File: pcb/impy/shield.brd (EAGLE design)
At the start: 133 x 107 mm, 117 parts, among them J1 USB-2410-06, J2 SI-60062-F, J3 5V, U1 AD5933YRS, U10 LTC3406AB, U11 23LCV1024-I/SN, U12 MIC2009A-1YM6, U13 ADG725BSU, U14 ADG725BSU, U2 ADG704BRM, U3 AD8656ARZ, U4 M24C08WMN, U5 ADG706BRU, U6 DP83848I, U7 MIC2009A-1YM6, U8 AT25DF081A-SS, U9 SST25VF080B-80-4I-S2

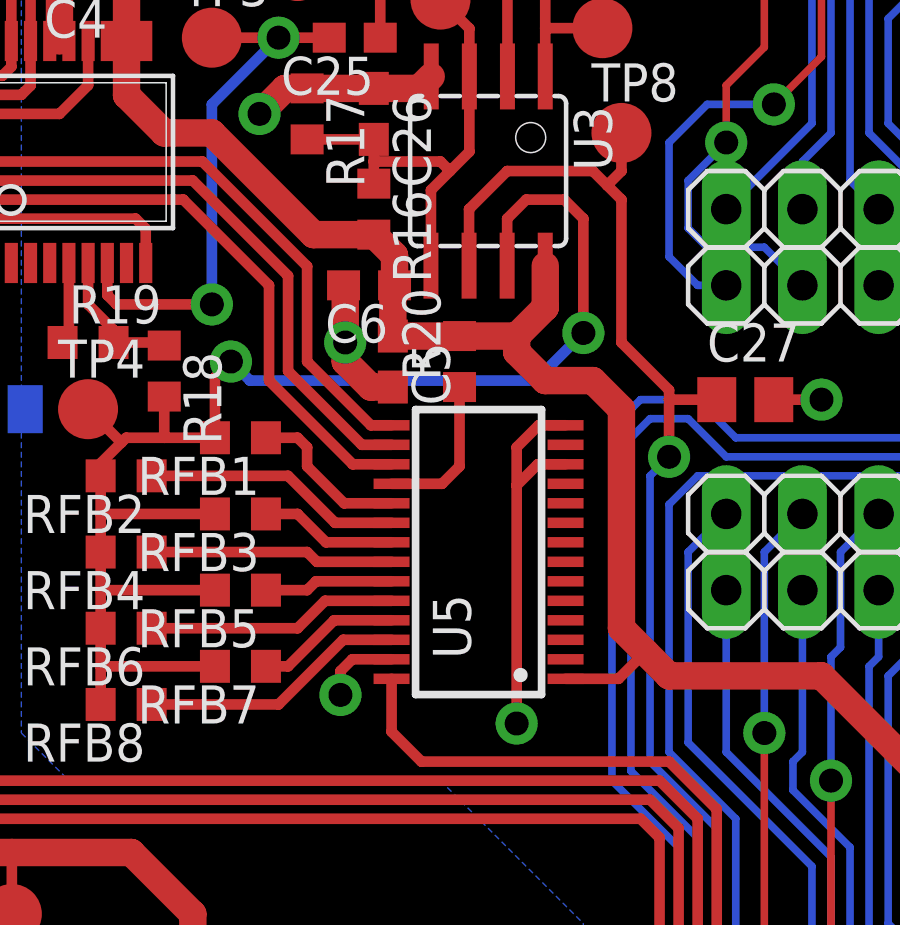
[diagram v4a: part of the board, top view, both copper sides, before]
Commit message: * pcb/impy: (shield.sch) Remove PE11 from discovery board header.   (shield.brd) Move some traces in preparation for feedback mux selection signal change.
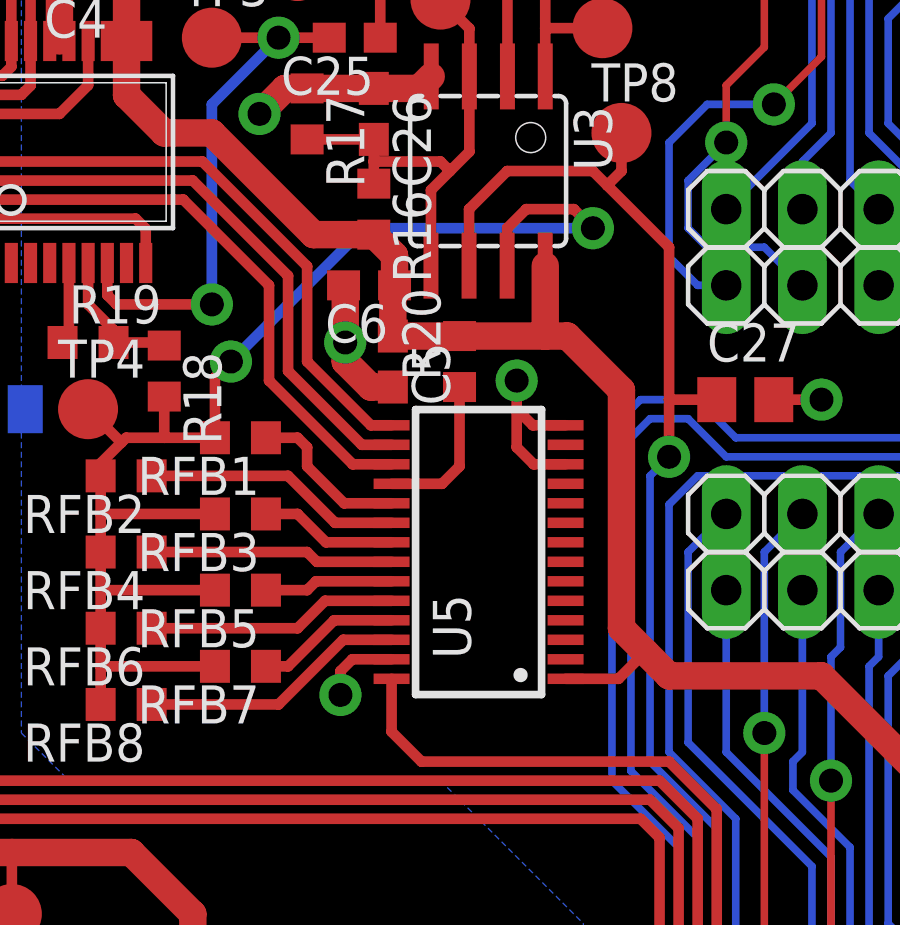
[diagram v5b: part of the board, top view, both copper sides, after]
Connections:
- removed net PE11: JP1.29
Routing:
- net AGND: track 55.1 -> 47.9 mm
- net N$1: track 50.4 -> 47.9 mm
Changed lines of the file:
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@@
 <wire x1="-20.6375" y1="29.21" x2="-27.6225" y2="29.21" width="0.3556" layer="1"/>
-</signal>
-<signal name="PE11">
-<contactref element="JP1" pad="29"/>
 </signal>
 <signal name="PE12">
@@
 <wire x1="89.8525" y1="89.7509" x2="89.8525" y2="82.3341" width="0.3556" layer="16"/>
 <wire x1="89.8525" y1="82.3341" x2="88.2015" y2="80.6831" width="0.3556" layer="16"/>
-<wire x1="56.515" y1="39.0735" x2="56.515" y2="37.68" width="0.9144" layer="1"/>
-<wire x1="56.515" y1="37.68" x2="55.5625" y2="36.7275" width="0.9144" layer="1"/>
 <wire x1="42.125" y1="48.5775" x2="42.5575" y2="48.145" width="0.9144" layer="1"/>
 <wire x1="42.5575" y1="48.145" x2="42.5575" y2="46.5625" width="0.9144" layer="1"/>
-<wire x1="55.5625" y1="36.7275" x2="53.6575" y2="36.7275" width="0.9144" layer="1"/>
+<wire x1="57.2525" y1="36.7275" x2="56.515" y2="36.7275" width="0.9144" layer="1"/>
+<wire x1="56.515" y1="36.7275" x2="53.6575" y2="36.7275" width="0.9144" layer="1"/>
 <wire x1="53.6575" y1="36.7275" x2="51.435" y2="36.7275" width="0.9144" layer="1"/>
 <wire x1="51.435" y1="36.7275" x2="51.435" y2="38.36125" width="0.9144" layer="1"/>
 <wire x1="51.435" y1="38.36125" x2="51.49125" y2="38.4175" width="0.9144" layer="1"/>
-<wire x1="55.5625" y1="36.7275" x2="55.5625" y2="36.195" width="0.9144" layer="1"/>
-<wire x1="55.5625" y1="36.195" x2="56.515" y2="35.2425" width="0.9144" layer="1"/>
-<wire x1="56.515" y1="35.2425" x2="58.1025" y2="35.2425" width="0.9144" layer="1"/>
-<wire x1="58.1025" y1="35.2425" x2="59.055" y2="34.29" width="0.9144" layer="1"/>
-<wire x1="59.055" y1="34.29" x2="59.055" y2="26.9875" width="0.9144" layer="1"/>
+<wire x1="59.055" y1="34.925" x2="59.055" y2="26.9875" width="0.9144" layer="1"/>
 <wire x1="59.055" y1="26.9875" x2="59.84875" y2="26.19375" width="0.9144" layer="1"/>
 <wire x1="59.84875" y1="26.19375" x2="60.6425" y2="25.4" width="0.9144" layer="1"/>
@@
 <wire x1="16.4075" y1="20.32" x2="17.205" y2="19.5225" width="0.3556" layer="1"/>
 <wire x1="17.205" y1="19.5225" x2="17.205" y2="18.7325" width="0.3556" layer="1"/>
+<wire x1="59.055" y1="34.925" x2="57.2525" y2="36.7275" width="0.9144" layer="1"/>
+<wire x1="56.515" y1="39.0735" x2="56.515" y2="36.7275" width="0.9144" layer="1"/>
 <wire x1="79.0575" y1="91.1225" x2="88.2015" y2="91.4019" width="0" layer="19" extent="16-16"/>
 <wire x1="66.675" y1="65.7225" x2="71.755" y2="81.495" width="0" layer="19" extent="1-16"/>
@@
 <wire x1="49.79125" y1="38.4175" x2="49.8475" y2="38.36125" width="0.9144" layer="1"/>
 <wire x1="49.8475" y1="38.36125" x2="49.8475" y2="36.5125" width="0.9144" layer="1"/>
-<wire x1="55.5625" y1="33.02" x2="55.5625" y2="31.75" width="0.3556" layer="1"/>
-<via x="55.5625" y="23.8125" extent="1-16" drill="0.8" shape="octagon"/>
-<wire x1="55.5625" y1="31.75" x2="55.5625" y2="23.8125" width="0.3556" layer="1"/>
 <wire x1="64.1325" y1="34.6075" x2="65.7225" y2="34.6075" width="0.3556" layer="1"/>
 <via x="65.7225" y="34.6075" extent="1-16" drill="0.8" shape="octagon"/>
 <contactref element="U5" pad="14"/>
-<wire x1="57.1925" y1="33.7525" x2="56.295" y2="33.7525" width="0.3556" layer="1"/>
-<wire x1="56.295" y1="33.7525" x2="55.5625" y2="33.02" width="0.3556" layer="1"/>
-<wire x1="57.1925" y1="32.4525" x2="56.265" y2="32.4525" width="0.3556" layer="1"/>
-<wire x1="56.265" y1="32.4525" x2="55.5625" y2="31.75" width="0.3556" layer="1"/>
+<wire x1="57.1925" y1="32.4525" x2="56.13" y2="32.4525" width="0.3556" layer="1"/>
+<wire x1="56.13" y1="32.4525" x2="55.5625" y2="33.02" width="0.3556" layer="1"/>
+<wire x1="55.5625" y1="33.02" x2="55.5625" y2="34.29" width="0.3556" layer="1"/>
+<wire x1="55.5625" y1="34.29" x2="55.5625" y2="35.2425" width="0.3556" layer="1"/>
+<via x="55.5625" y="35.2425" extent="1-16" drill="0.8" shape="octagon"/>
+<wire x1="57.1925" y1="33.7525" x2="56.1" y2="33.7525" width="0.3556" layer="1"/>
+<wire x1="56.1" y1="33.7525" x2="55.5625" y2="34.29" width="0.3556" layer="1"/>
 </signal>
 <signal name="PA2">
@@
 <wire x1="41.695" y1="32.0675" x2="41.695" y2="32.4875" width="0.3556" layer="1"/>
 <wire x1="41.275" y1="34.29" x2="42.38625" y2="33.17875" width="0.3556" layer="1"/>
-<wire x1="55.245" y1="39.0735" x2="55.245" y2="40.64" width="0.3556" layer="1"/>
-<wire x1="55.245" y1="40.64" x2="55.88" y2="41.275" width="0.3556" layer="1"/>
-<wire x1="55.88" y1="41.275" x2="57.15" y2="41.275" width="0.3556" layer="1"/>
-<wire x1="57.15" y1="41.275" x2="57.785" y2="40.64" width="0.3556" layer="1"/>
-<wire x1="57.785" y1="40.64" x2="57.785" y2="36.83" width="0.3556" layer="1"/>
-<via x="57.785" y="36.83" extent="1-16" drill="0.8" shape="octagon"/>
-<wire x1="57.785" y1="36.83" x2="56.1975" y2="35.2425" width="0.3556" layer="16"/>
-<wire x1="56.1975" y1="35.2425" x2="46.6725" y2="35.2425" width="0.3556" layer="16"/>
-<wire x1="46.6725" y1="35.2425" x2="46.0375" y2="35.8775" width="0.3556" layer="16"/>
+<wire x1="55.245" y1="39.0735" x2="55.245" y2="40.3225" width="0.3556" layer="1"/>
+<wire x1="55.245" y1="40.3225" x2="55.88" y2="40.9575" width="0.3556" layer="1"/>
+<wire x1="55.88" y1="40.9575" x2="57.4675" y2="40.9575" width="0.3556" layer="1"/>
+<via x="58.1025" y="40.3225" extent="1-16" drill="0.8" shape="octagon"/>
 <via x="46.0375" y="35.8775" extent="1-16" drill="0.8" shape="octagon"/>
 <wire x1="46.0375" y1="35.8775" x2="45.505" y2="35.345" width="0.3556" layer="1"/>
 <wire x1="45.505" y1="35.345" x2="45.505" y2="33.3375" width="0.3556" layer="1"/>
+<wire x1="46.0375" y1="35.8775" x2="50.4825" y2="40.3225" width="0.3556" layer="16"/>
+<wire x1="50.4825" y1="40.3225" x2="58.1025" y2="40.3225" width="0.3556" layer="16"/>
+<wire x1="57.4675" y1="40.9575" x2="58.1025" y2="40.3225" width="0.3556" layer="1"/>
 </signal>
 <signal name="N$12" class="2">
@@
 <wire x1="58.1025" y1="42.2275" x2="58.57875" y2="41.75125" width="0.3556" layer="1"/>
 <via x="60.6425" y="32.7025" extent="1-16" drill="0.8" shape="octagon"/>
-<wire x1="58.57875" y1="41.75125" x2="59.055" y2="41.275" width="0.3556" layer="1"/>
-<wire x1="59.055" y1="41.275" x2="59.055" y2="36.5125" width="0.3556" layer="1"/>
+<wire x1="58.57875" y1="41.75125" x2="60.6425" y2="39.6875" width="0.3556" layer="1"/>
+<wire x1="60.6425" y1="39.6875" x2="60.6425" y2="34.6075" width="0.3556" layer="1"/>
 <wire x1="59.055" y1="43.4975" x2="59.055" y2="42.2275" width="0.3556" layer="1"/>
 <wire x1="59.055" y1="42.2275" x2="58.57875" y2="41.75125" width="0.3556" layer="1"/>
 <wire x1="60.6425" y1="32.7025" x2="60.6425" y2="34.6075" width="0.3556" layer="1"/>
-<wire x1="60.6425" y1="34.6075" x2="60.6425" y2="34.925" width="0.3556" layer="1"/>
-<wire x1="60.6425" y1="34.925" x2="59.055" y2="36.5125" width="0.3556" layer="1"/>
 <wire x1="60.0075" y1="22.5425" x2="60.0075" y2="32.0675" width="0.254" layer="16"/>
 <wire x1="60.0075" y1="32.0675" x2="60.6425" y2="32.7025" width="0.254" layer="16"/>

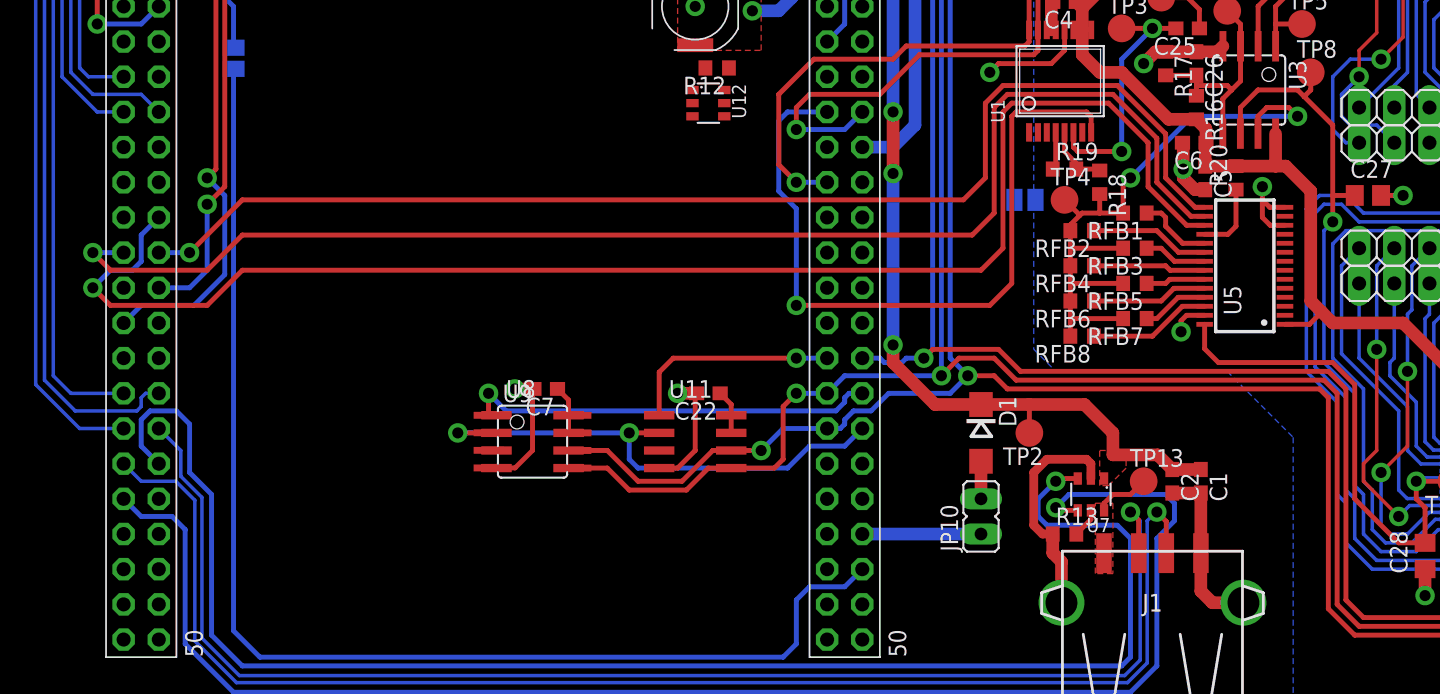
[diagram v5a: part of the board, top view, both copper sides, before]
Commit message: * pcb/impy: (shield.sch, shield.brd) Change feedback mux selection signals (PE8, PE9, PE10 to PB4, PB5, PB7) and layout.
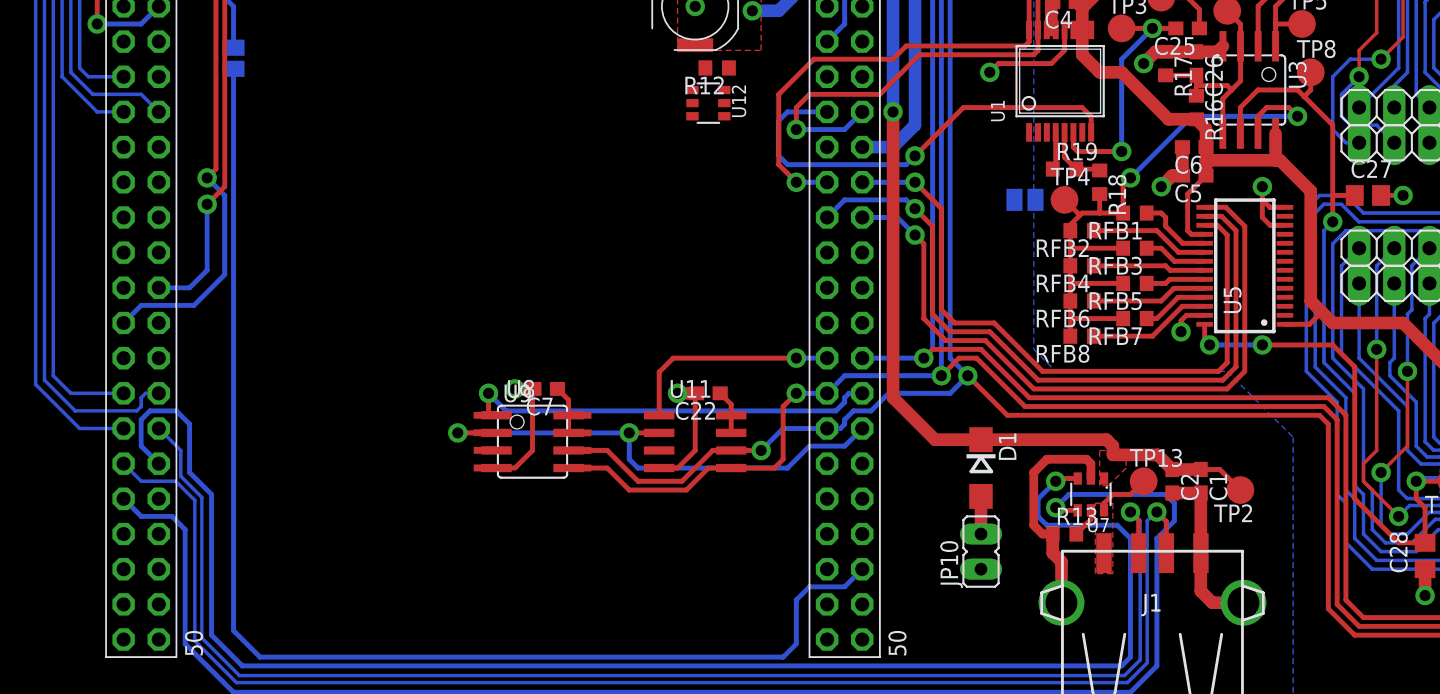
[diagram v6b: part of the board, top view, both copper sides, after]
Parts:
- removed R20: 10k, rcl:R0603
- moved TP2 15.8 mm to (54.0, 13.3)
- moved D1 2.54 mm to (35.2, 14.9)
- moved JP10 2.54 mm to (35.2, 8.89)
- moved C5 0.81 mm to (50.6, 36.0), turned to 180 degrees
- moved C6 0.32 mm to (50.6, 38.1)
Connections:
- removed net N$107: R20.1, U5.18
- removed net PE10: JP1.28, U5.15
- removed net PE8: JP1.26, U5.17
- removed net PE9: JP1.27, U5.16
- new net PB4: JP2.25, U5.16
- new net PB5: JP2.26, U5.15
- new net PB7: JP2.24, U5.17
- net VCC: now also U5.18; no longer R20.2
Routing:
- net PE8: track 106.1 -> 0.00 mm, vias 1 -> 0
- net PE9: track 98.3 -> 0.00 mm, vias 1 -> 0
- net PE10: track 89.2 -> 0.00 mm, vias 1 -> 0
- net PB4: track 0.00 -> 52.1 mm, vias 0 -> 1
- net PB5: track 0.00 -> 50.4 mm, vias 0 -> 1
- net PB7: track 0.00 -> 47.7 mm, vias 0 -> 1
- net PB8: track 53.0 -> 32.2 mm
- net PA9: track 8.57 -> 0.00 mm
- net VCC: track 204.0 -> 210.5 mm
- net N$107: track 5.15 -> 0.00 mm
- net +5V: track 138.7 -> 141.0 mm, vias 9 -> 7
- net PD2: track 179.5 -> 178.1 mm
- net PC10: track 200.6 -> 199.5 mm
- net PC12: track 204.7 -> 203.6 mm
- net AGND: track 47.9 -> 47.4 mm
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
